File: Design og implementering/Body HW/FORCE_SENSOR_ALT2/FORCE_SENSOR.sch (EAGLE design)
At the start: 15 parts, among them IC1 MCP6004P, J1 RJ11-6PTH, J2 RJ11-6PTH

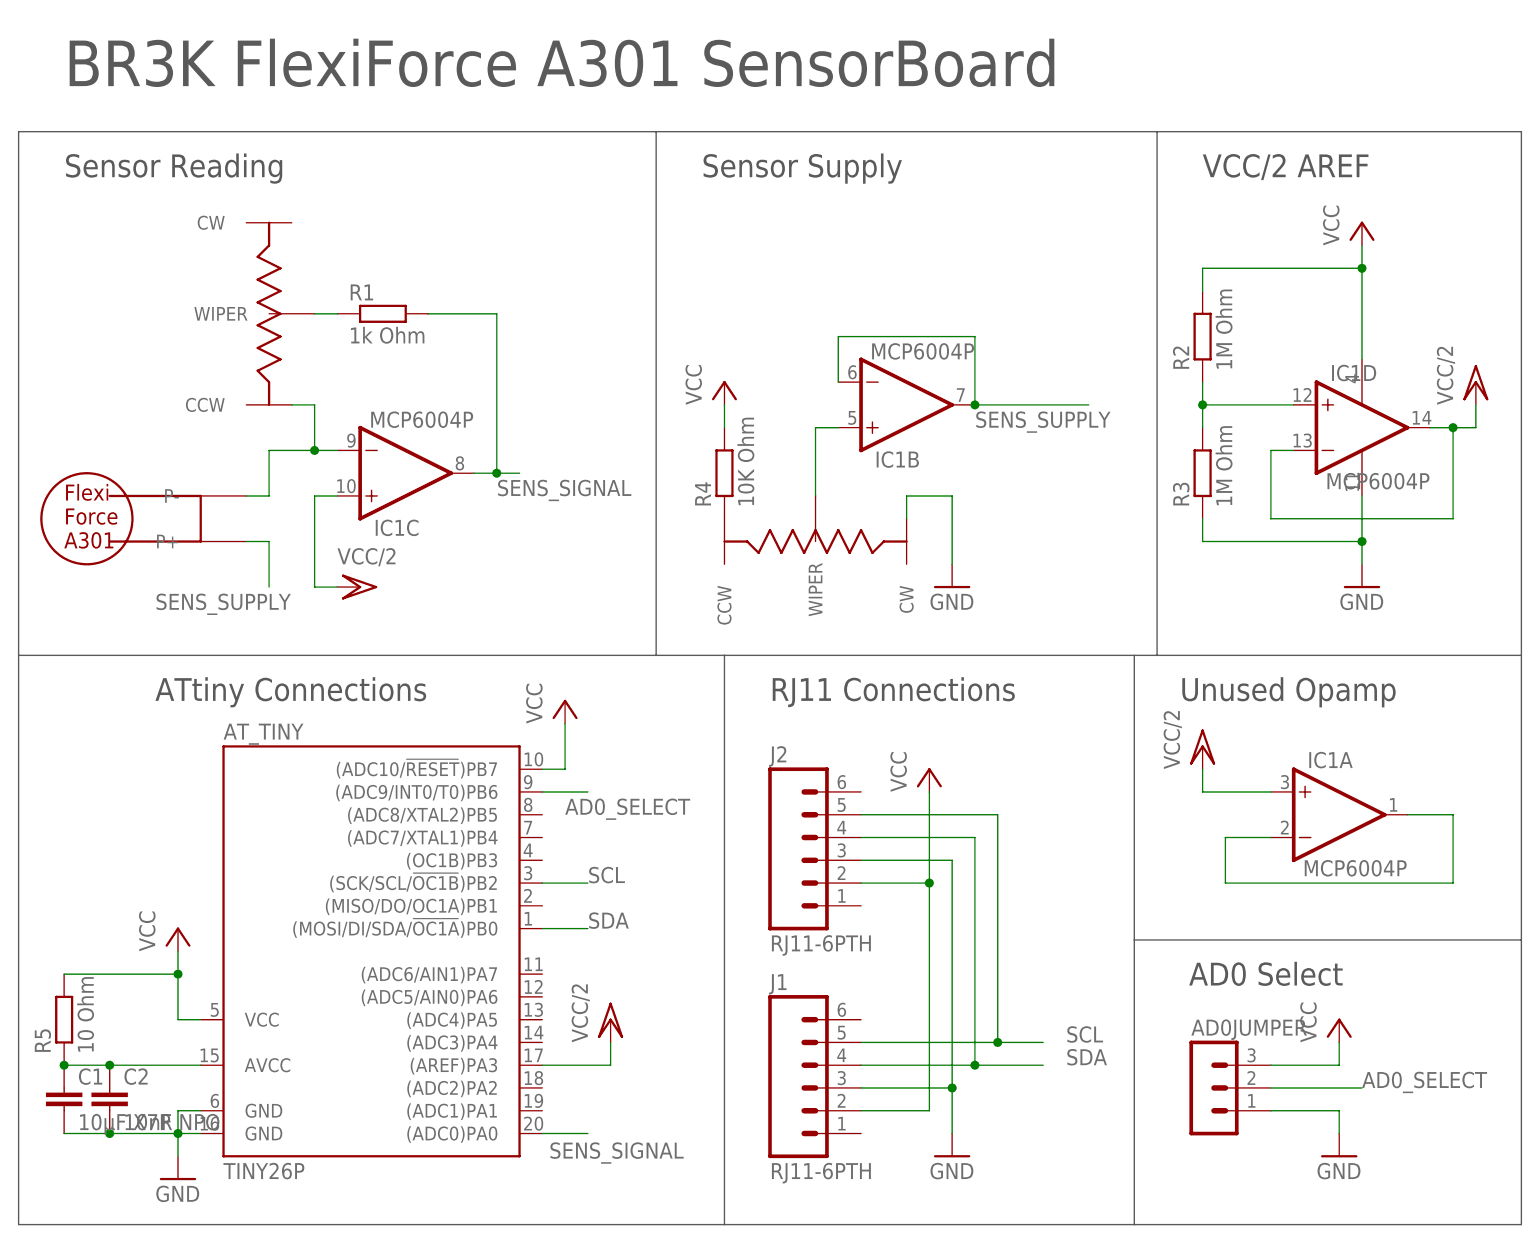
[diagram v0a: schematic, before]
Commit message: Added improved Force sensor design -Felix
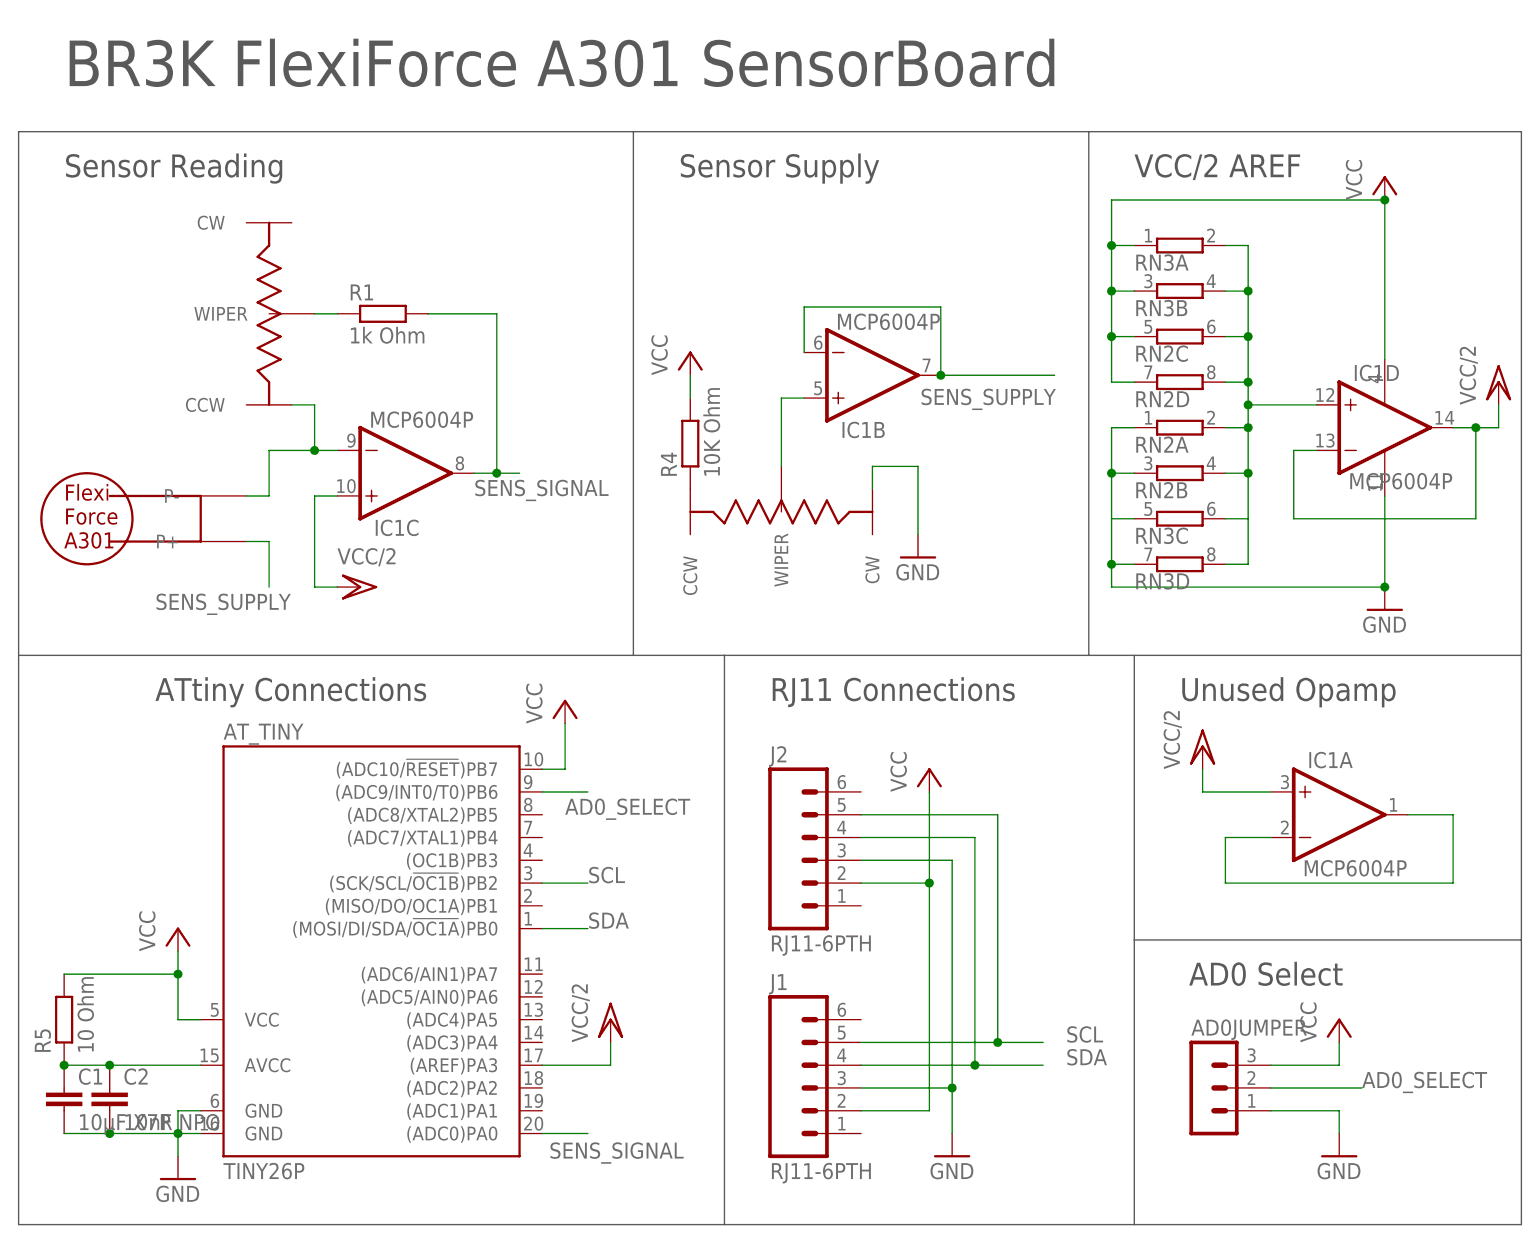
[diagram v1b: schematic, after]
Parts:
- removed R2, R3: 1M Ohm, resistor:R-EU_0207_10
- added RN2, RN3: (no value), resistor-sil:E4R
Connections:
- removed net N$2: IC1D.+IN, R2.1, R3.2
- new net N$11: IC1D.+IN, RN2A.2, RN2B.2, RN2C.2, RN2D.2, RN3A.2, RN3B.2, RN3C.2, RN3D.2
- net GND: now also RN2A.1, RN2B.1, RN3C.1, RN3D.1; no longer R3.1
- net VCC: now also RN2C.1, RN2D.1, RN3A.1, RN3B.1; no longer R2.2
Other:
- moved on the sheet: IC1B, IC1D, R4

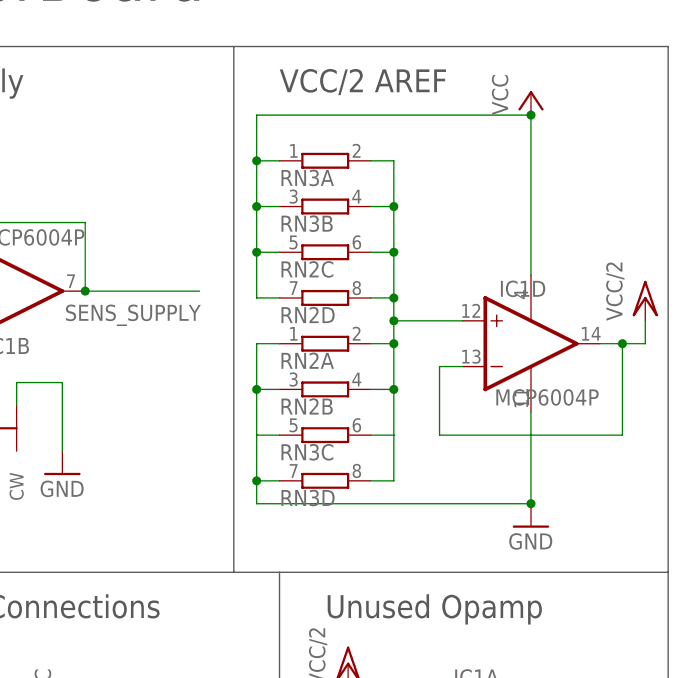
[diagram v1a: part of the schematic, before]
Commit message: Finished the Force Sensor circuit and sent it and the mpu6050 board for production -Felix
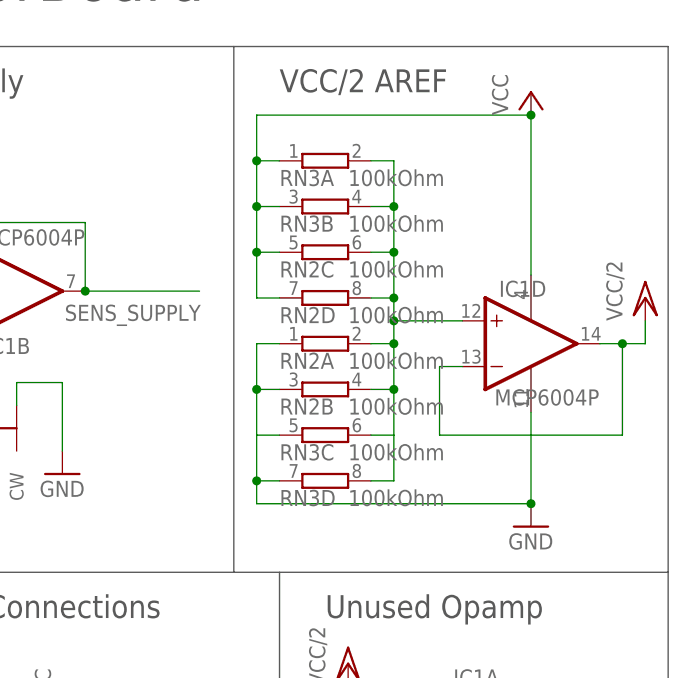
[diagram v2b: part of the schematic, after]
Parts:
- RN2, RN3: value (none) -> 100kOhm
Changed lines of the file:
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@@
 <part name="C2" library="capacitor-wima" deviceset="C" device="5/2.5" value="10nF NPO"/>
 <part name="R5" library="resistor" deviceset="R-EU_" device="0207_10" value="10 Ohm"/>
-<part name="RN2" library="resistor-sil" deviceset="E4R" device=""/>
-<part name="RN3" library="resistor-sil" deviceset="E4R" device=""/>
+<part name="RN2" library="resistor-sil" deviceset="E4R" device="" value="100kOhm"/>
+<part name="RN3" library="resistor-sil" deviceset="E4R" device="" value="100kOhm"/>
 </parts>
 <sheets>
